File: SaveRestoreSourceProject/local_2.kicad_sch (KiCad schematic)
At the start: 6 parts

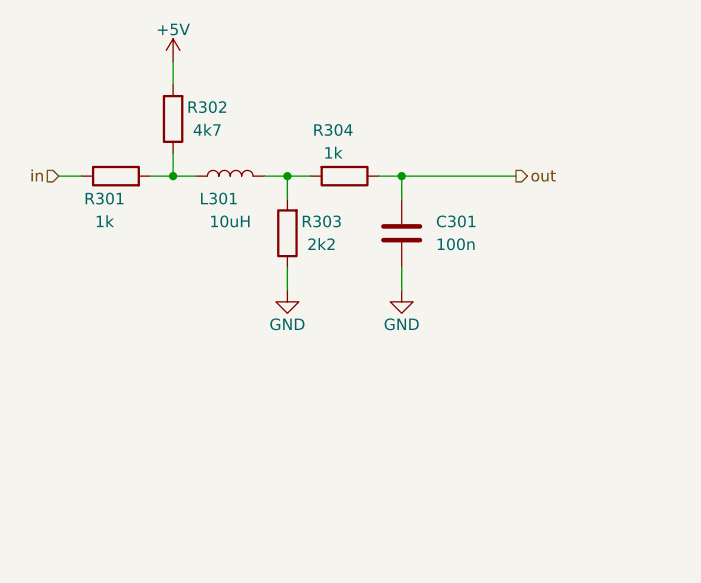
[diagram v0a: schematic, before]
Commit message: Add support for connected drawings, update test template
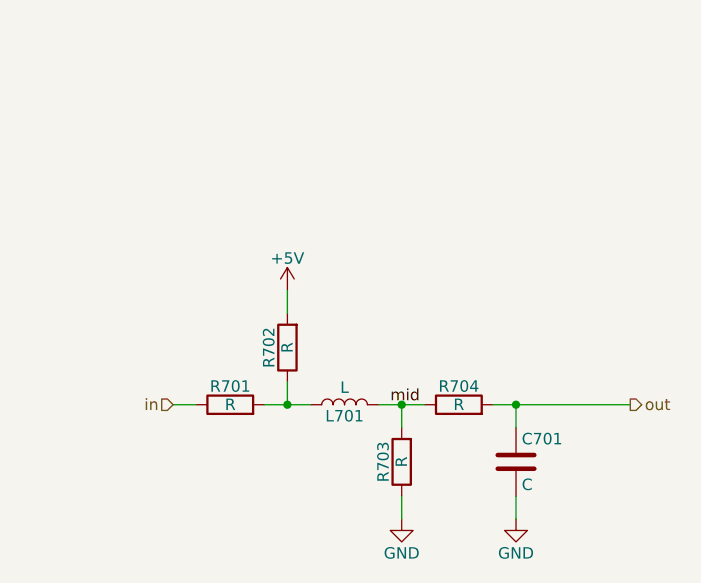
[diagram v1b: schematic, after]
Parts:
- removed C301: 100n, Capacitor_SMD:C_1206_3216Metric_Pad1.33x1.80mm_HandSolder, symbol Device:C
- removed L301: 10uH, Inductor_SMD:L_1206_3216Metric_Pad1.22x1.90mm_HandSolder, symbol Device:L
- removed R301, R304: 1k, Resistor_SMD:R_1206_3216Metric, symbol Device:R
- removed R302: 4k7, Resistor_SMD:R_1206_3216Metric, symbol Device:R
- removed R303: 2k2, Resistor_SMD:R_1206_3216Metric, symbol Device:R
- added C701: C, Capacitor_SMD:C_1206_3216Metric, symbol Device:C
- added L701: L, Inductor_SMD:L_1206_3216Metric, symbol Device:L
- added R701, R702, R703, R704: R, Resistor_SMD:R_1206_3216Metric, symbol Device:R
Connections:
- net +5V: now also R702.2
- net GND: now also C701.2, R703.1
- net in: now also R701.1
- net out: now also C701.1, R704.2
- new net: L701.1, R701.2, R702.1
- new net mid: L701.2, R703.2, R704.1
